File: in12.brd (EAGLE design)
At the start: 146.1 x 33.7 mm, 28 parts, among them J1 1-2328702-0

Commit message: routing connector
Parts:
- moved J1 0.54 mm to (5.71, 26.0)
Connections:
- net 3V3: now also J1.9; no longer J1.6
- net BL: now also J1.7; no longer J1.9
- net GND: now also J1.10; no longer J1.5
- net IN: now also J1.6; no longer J1.8
- net LE: now also J1.5; no longer J1.7
- net OUT: now also J1.8; no longer J1.10
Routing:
- net HV: track 171.1 -> 175.6 mm
- net L14: track 23.9 -> 23.2 mm
- net L13: track 27.2 -> 26.5 mm
- net L12: track 30.4 -> 29.8 mm
- net BL: track 0.00 -> 0.65 mm
- net POL: track 0.00 -> 0.59 mm
- net L10: track 52.1 -> 51.5 mm

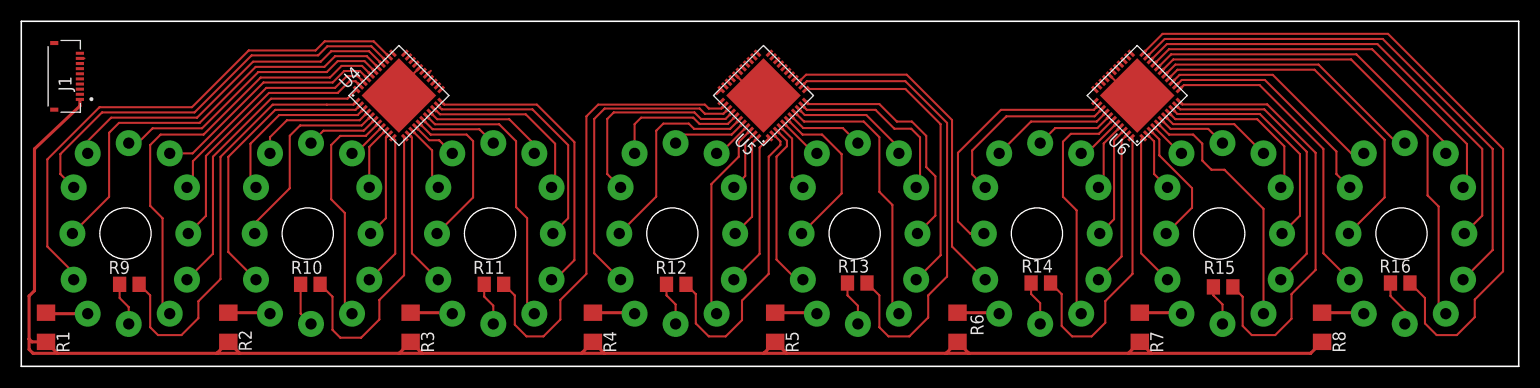
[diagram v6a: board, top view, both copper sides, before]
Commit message: lamp board finished, working on control
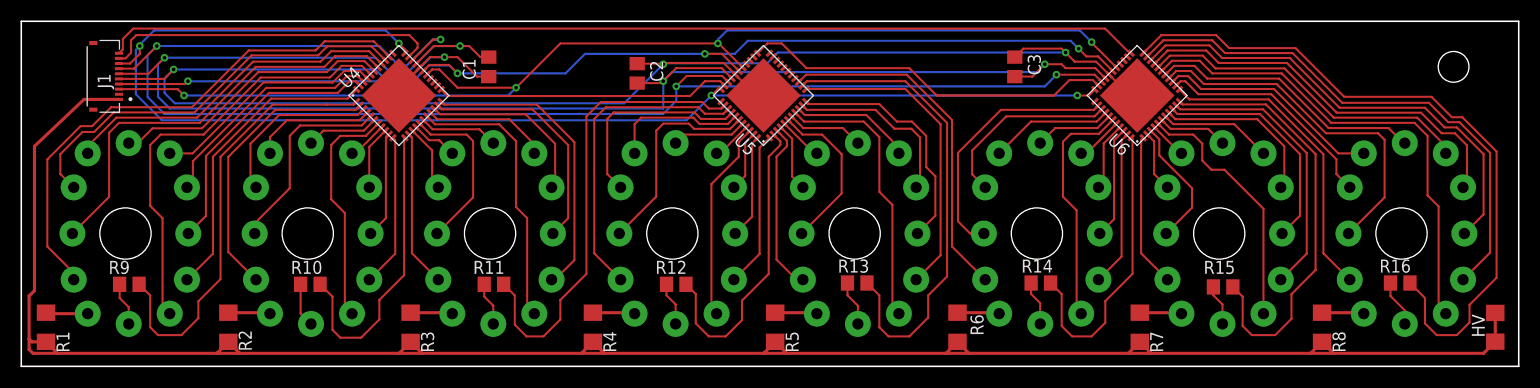
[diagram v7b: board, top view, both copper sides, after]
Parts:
- added C1, C2, C3: (no value), rcl:C0805
- added HV: (no value), rcl:C1206
- moved J1 3.81 mm to (9.53, 26.0)
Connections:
- net 3V3: now also C1.2, C2.2, C3.2, J1.6; no longer J1.9
- net BL: now also J1.8; no longer J1.7
- net GND: now also C1.1, C2.1, C3.1, J1.5; no longer J1.10
- net HV: now also HV.1, HV.2
- net IN: now also J1.9; no longer J1.6
- net LE: now also J1.7; no longer J1.5
- net OUT: now also J1.10; no longer J1.8
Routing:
- net 3V3: track 0.44 -> 158.8 mm, vias 0 -> 4
- net GND: track 10.6 -> 165.5 mm, vias 0 -> 4
- net LE: track 0.00 -> 145.4 mm, vias 0 -> 4
- net BL: track 0.65 -> 132.9 mm, vias 0 -> 4
- net POL: track 0.59 -> 115.1 mm, vias 0 -> 4
- net CLK: track 0.00 -> 108.6 mm, vias 0 -> 4
- net OUT: track 0.00 -> 101.3 mm
- net N$18: track 0.00 -> 36.6 mm
- net IN: track 0.00 -> 32.8 mm
- net N$17: track 0.00 -> 28.7 mm
- net HV: track 175.6 -> 202.0 mm
- net L8D: track 68.7 -> 67.5 mm
- net L82: track 52.9 -> 52.2 mm
- net L80: track 30.6 -> 30.0 mm
- net L88: track 22.8 -> 22.3 mm

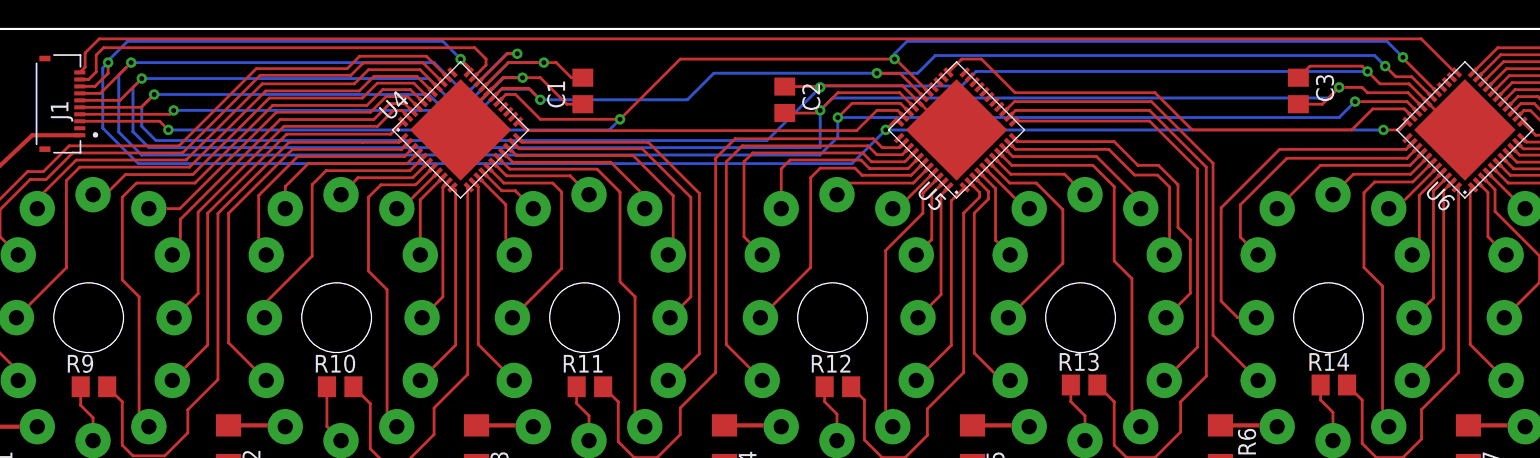
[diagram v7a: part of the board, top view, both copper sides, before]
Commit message: add readme, brushup board
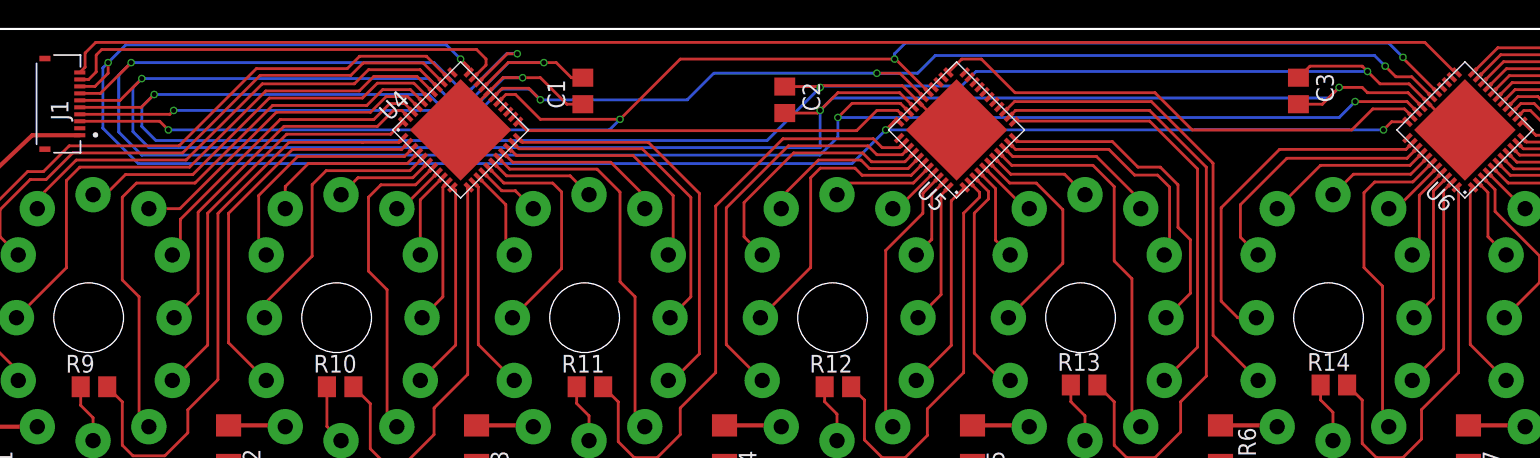
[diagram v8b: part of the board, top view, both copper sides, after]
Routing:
- net L3D: track 45.3 -> 43.3 mm
- net L40: track 30.8 -> 28.8 mm
- net L48: track 20.2 -> 18.5 mm
- net L47: track 13.6 -> 12.4 mm
